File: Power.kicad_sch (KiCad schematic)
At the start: 48 parts, among them SW901 DP3T, U901 BQ24075, U902 TPS7A0533PDBV, U903 LP5907MFX-3.3

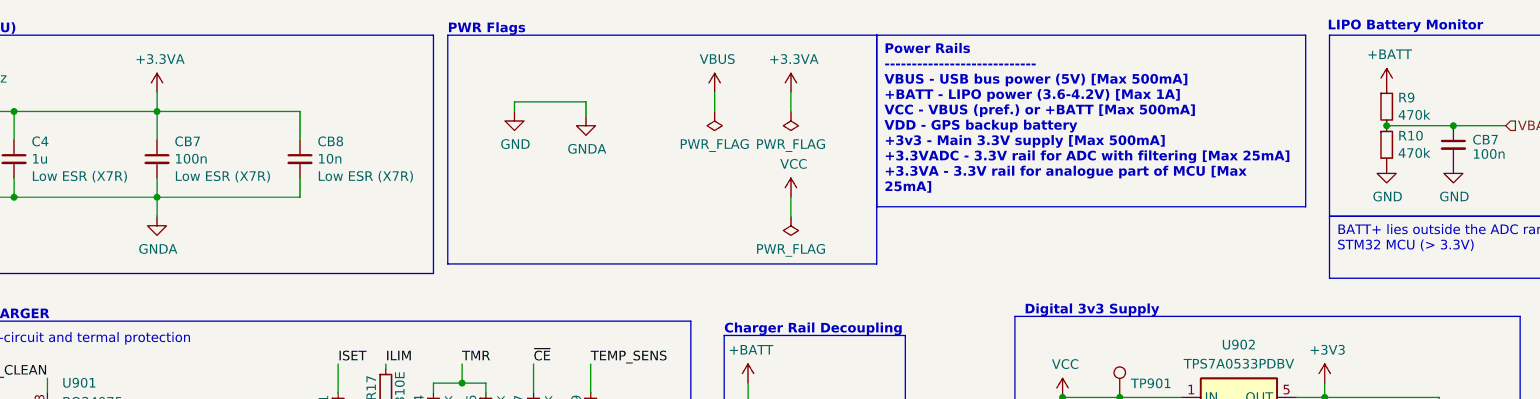
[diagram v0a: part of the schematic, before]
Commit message: (sch) replace GNDA with GND
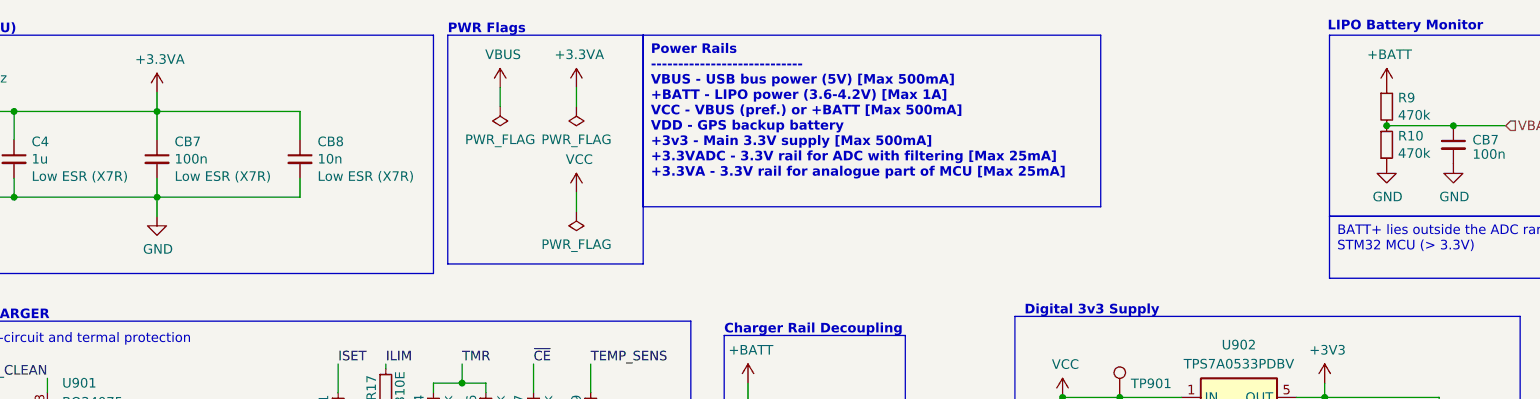
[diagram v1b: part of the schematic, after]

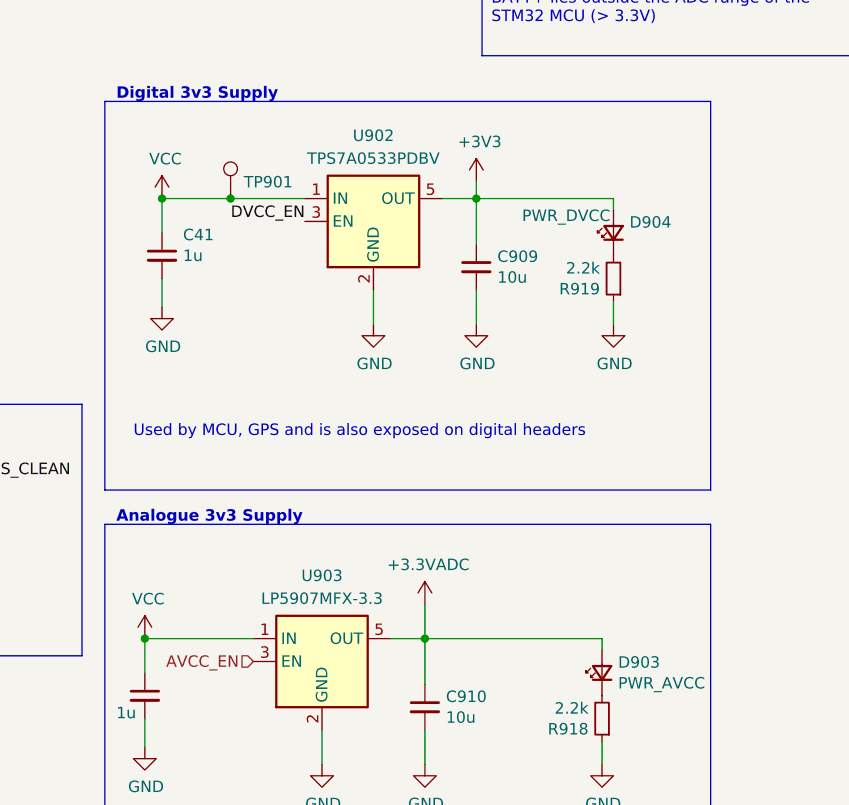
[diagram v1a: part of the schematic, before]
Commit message: (sch) add power test points
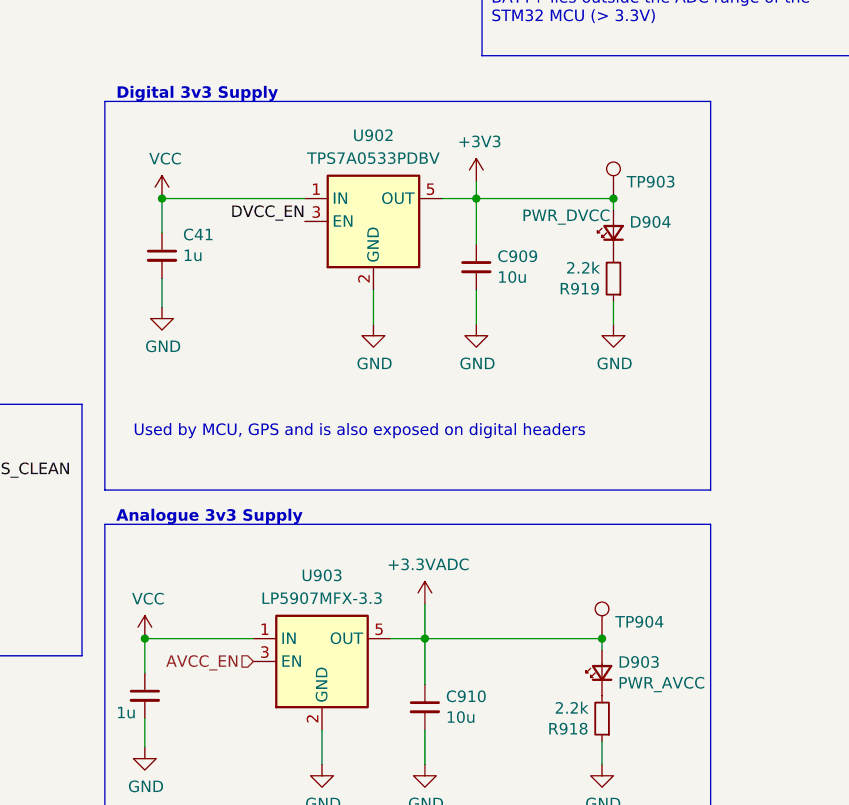
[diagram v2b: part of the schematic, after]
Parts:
- removed TP901: VIN, TestPoint:TestPoint_Pad_D1.0mm, symbol Connector:TestPoint
- added TP903, TP904: VIN, TestPoint:TestPoint_Pad_D1.0mm, symbol Connector:TestPoint
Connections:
- net +3.3VADC: now also TP904.1
- net +3V3: now also TP903.1
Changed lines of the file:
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@@
   (junction (at 57.15 26.67) (diameter 0) (color 0 0 0 0)
   )
+  (junction (at 226.695 113.665) (diameter 0) (color 0 0 0 0)
+  )
   (junction (at 207.01 113.665) (diameter 0) (color 0 0 0 0)
   )
@@
   (junction (at 249.555 28.575) (diameter 0) (color 0 0 0 0)
   )
+  (junction (at 227.965 64.77) (diameter 0) (color 0 0 0 0)
+  )
   (junction (at 212.725 64.77) (diameter 0) (color 0 0 0 0)
   )
@@
   (junction (at 38.1 38.1) (diameter 0) (color 0 0 0 0)
   )
-  (junction (at 185.42 64.77) (diameter 0) (color 0 0 0 0)
-  )
   (junction (at 258.445 28.575) (diameter 0) (color 0 0 0 0)
   )
@@
     (stroke (width 0) (type default))
   )
-  (wire (pts (xy 185.42 64.77) (xy 193.675 64.77))
+  (wire (pts (xy 177.8 64.77) (xy 193.675 64.77))
     (stroke (width 0) (type default))
   )
@@
     (stroke (width 0) (type default))
   )
-  (wire (pts (xy 177.8 64.77) (xy 185.42 64.77))
-    (stroke (width 0) (type default))
-  )
   (wire (pts (xy 107.315 60.325) (xy 107.315 64.135))
     (stroke (width 0) (type default))
@@
     )
   )
+  (symbol (lib_id "Connector:TestPoint") (at 226.695 113.665 0) (unit 1)
+    (in_bom yes) (on_board yes) (dnp no)
+    (property "Reference" "TP904" (at 228.1682 111.8362 0)
+      (effects (font (size 1.27 1.27)) (justify left))
+    )
+    (property "Value" "VIN" (at 228.1682 112.9792 0)
+      (effects (font (size 1.27 1.27)) (justify left) hide)
+    )
+    (property "Footprint" "TestPoint:TestPoint_Pad_D1.0mm" (at 231.775 113.665 0)
+      (effects (font (size 1.27 1.27)) hide)
+    )
+    (property "Datasheet" "~" (at 231.775 113.665 0)
+      (effects (font (size 1.27 1.27)) hide)
+    )
+    (pin "1")
+    (instances
+      (project "kleinvoet"
+        (path "/4185c36c-c66e-4dbd-be5d-841e551f4885/00000000-0000-0000-0000-00005eede770"
+          (reference "TP904") (unit 1)
+        )
+      )
+    )
+  )
   (symbol (lib_id "Device:C_Small") (at 212.725 72.39 0) (unit 1)
     (in_bom yes) (on_board yes) (dnp no)
@@
     )
   )
-  (symbol (lib_id "Connector:TestPoint") (at 185.42 64.77 0) (unit 1)
-    (in_bom yes) (on_board yes) (dnp no)
-    (property "Reference" "TP901" (at 186.8932 62.9412 0)
-      (effects (font (size 1.27 1.27)) (justify left))
-    )
-    (property "Value" "VIN" (at 186.8932 64.0842 0)
-      (effects (font (size 1.27 1.27)) (justify left) hide)
-    )
-    (property "Footprint" "TestPoint:TestPoint_Pad_D1.0mm" (at 190.5 64.77 0)
-      (effects (font (size 1.27 1.27)) hide)
-    )
-    (property "Datasheet" "~" (at 190.5 64.77 0)
-      (effects (font (size 1.27 1.27)) hide)
-    )
-    (pin "1")
-    (instances
-      (project "kleinvoet"
-        (path "/4185c36c-c66e-4dbd-be5d-841e551f4885/00000000-0000-0000-0000-00005eede770"
-          (reference "TP901") (unit 1)
-        )
-      )
-    )
-  )
   (symbol (lib_id "Device:R_Small") (at 78.105 165.1 90) (unit 1)
     (in_bom yes) (on_board yes) (dnp no)
@@
         )
       )
+    )
+  )
+  (symbol (lib_id "Connector:TestPoint") (at 227.965 64.77 0) (unit 1)
+    (in_bom yes) (on_board yes) (dnp no)
+    (property "Reference" "TP903" (at 229.4382 62.9412 0)
+      (effects (font (size 1.27 1.27)) (justify left))
+    )
+    (property "Value" "VIN" (at 229.4382 64.0842 0)
+      (effects (font (size 1.27 1.27)) (justify left) hide)
+    )
+    (property "Footprint" "TestPoint:TestPoint_Pad_D1.0mm" (at 233.045 64.77 0)
+      (effects (font (size 1.27 1.27)) hide)
+    )
+    (property "Datasheet" "~" (at 233.045 64.77 0)
+      (effects (font (size 1.27 1.27)) hide)
+    )
+    (pin "1")
+    (instances
+      (project "kleinvoet"
+        (path "/4185c36c-c66e-4dbd-be5d-841e551f4885/00000000-0000-0000-0000-00005eede770"
+          (reference "TP903") (unit 1)
+        )
+      )

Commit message: change 10u cap from 0805 to 0402
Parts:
- C903, C904, C908, C909, C910: footprint Capacitor_SMD:C_0805_2012Metric_Pad1.18x1.45mm_HandSolder -> Capacitor_SMD:C_0402_1005Metric; MPN C0805C106K9PACTU -> GRM155R60J106ME05D; Mfr. KEMET -> Murata
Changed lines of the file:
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@@
       (effects (font (size 1.27 1.27)) (justify left))
     )
-    (property "Footprint" "Capacitor_SMD:C_0805_2012Metric_Pad1.18x1.45mm_HandSolder" (at 207.01 121.285 0)
+    (property "Footprint" "Capacitor_SMD:C_0402_1005Metric" (at 207.01 121.285 0)
       (effects (font (size 1.27 1.27)) hide)
     )
@@
       (effects (font (size 1.27 1.27)) hide)
     )
-    (property "MPN" "C0805C106K9PACTU" (at 207.01 121.285 0)
-      (effects (font (size 1.27 1.27)) hide)
-    )
-    (property "Mfr." "KEMET" (at 207.01 121.285 0)
+    (property "MPN" "GRM155R60J106ME05D" (at 207.01 121.285 0)
+      (effects (font (size 1.27 1.27)) hide)
+    )
+    (property "Mfr." "Murata" (at 207.01 121.285 0)
       (effects (font (size 1.27 1.27)) hide)
     )
@@
       (effects (font (size 1.27 1.27)) (justify left))
     )
-    (property "Footprint" "Capacitor_SMD:C_0805_2012Metric_Pad1.18x1.45mm_HandSolder" (at 137.16 102.235 0)
+    (property "Footprint" "Capacitor_SMD:C_0402_1005Metric" (at 137.16 102.235 0)
       (effects (font (size 1.27 1.27)) hide)
     )
@@
       (effects (font (size 1.27 1.27)) hide)
     )
-    (property "MPN" "C0805C106K9PACTU" (at 137.16 102.235 0)
-      (effects (font (size 1.27 1.27)) hide)
-    )
-    (property "Mfr." "KEMET" (at 137.16 102.235 0)
+    (property "MPN" "GRM155R60J106ME05D" (at 137.16 102.235 0)
+      (effects (font (size 1.27 1.27)) hide)
+    )
+    (property "Mfr." "Murata" (at 137.16 102.235 0)
       (effects (font (size 1.27 1.27)) hide)
     )
@@
       (effects (font (size 1.27 1.27)) (justify left))
     )
-    (property "Footprint" "Capacitor_SMD:C_0805_2012Metric_Pad1.18x1.45mm_HandSolder" (at 135.89 69.215 0)
+    (property "Footprint" "Capacitor_SMD:C_0402_1005Metric" (at 135.89 69.215 0)
       (effects (font (size 1.27 1.27)) hide)
     )
@@
       (effects (font (size 1.27 1.27)) hide)
     )
-    (property "MPN" "C0805C106K9PACTU" (at 135.89 69.215 0)
-      (effects (font (size 1.27 1.27)) hide)
-    )
-    (property "Mfr." "KEMET" (at 135.89 69.215 0)
+    (property "MPN" "GRM155R60J106ME05D" (at 135.89 69.215 0)
+      (effects (font (size 1.27 1.27)) hide)
+    )
+    (property "Mfr." "Murata" (at 135.89 69.215 0)
       (effects (font (size 1.27 1.27)) hide)
     )
@@
       (effects (font (size 1.27 1.27)) (justify left))
     )
-    (property "Footprint" "Capacitor_SMD:C_0805_2012Metric_Pad1.18x1.45mm_HandSolder" (at 149.86 102.235 0)
+    (property "Footprint" "Capacitor_SMD:C_0402_1005Metric" (at 149.86 102.235 0)
       (effects (font (size 1.27 1.27)) hide)
     )
@@
       (effects (font (size 1.27 1.27)) hide)
     )
-    (property "MPN" "C0805C106K9PACTU" (at 149.86 102.235 0)
-      (effects (font (size 1.27 1.27)) hide)
-    )
-    (property "Mfr." "KEMET" (at 149.86 102.235 0)
+    (property "MPN" "GRM155R60J106ME05D" (at 149.86 102.235 0)
+      (effects (font (size 1.27 1.27)) hide)
+    )
+    (property "Mfr." "Murata" (at 149.86 102.235 0)
       (effects (font (size 1.27 1.27)) hide)
     )
@@
       (effects (font (size 1.27 1.27)) (justify left))
     )
-    (property "Footprint" "Capacitor_SMD:C_0805_2012Metric_Pad1.18x1.45mm_HandSolder" (at 212.725 72.39 0)
+    (property "Footprint" "Capacitor_SMD:C_0402_1005Metric" (at 212.725 72.39 0)
       (effects (font (size 1.27 1.27)) hide)
     )
@@
       (effects (font (size 1.27 1.27)) hide)
     )
-    (property "MPN" "C0805C106K9PACTU" (at 212.725 72.39 0)
-      (effects (font (size 1.27 1.27)) hide)
-    )
-    (property "Mfr." "KEMET" (at 212.725 72.39 0)
-      (effects (font (size 1.27 1.27)) hide)
-    )
+    (property "MPN" "GRM155R60J106ME05D" (at 212.725 72.39 0)
+      (effects (font (size 1.27 1.27)) hide)
+    )
+    (property "Mfr." "Murata" (at 212.725 72.39 0)
+      (effects (font (size 1.27 1.27)) hide)
+    )

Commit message: replace passives with 0402
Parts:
- C4, C41: footprint Capacitor_SMD:C_0603_1608Metric_Pad1.08x0.95mm_HandSolder -> Capacitor_SMD:C_0402_1005Metric; MPN C0603C105K8RACTU -> C0402C105K9PACTU
- FB901, FB903: footprint Inductor_SMD:L_0603_1608Metric_Pad1.05x0.95mm_HandSolder -> Inductor_SMD:L_0402_1005Metric; MPN BLM18KG101TZ1D -> BLM15HD102SN1D
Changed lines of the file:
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@@
       (effects (font (size 1.27 1.27)))
     )
-    (property "Footprint" "Inductor_SMD:L_0603_1608Metric_Pad1.05x0.95mm_HandSolder" (at 30.48 28.448 90)
+    (property "Footprint" "Inductor_SMD:L_0402_1005Metric" (at 30.48 28.448 90)
       (effects (font (size 1.27 1.27)) hide)
     )
@@
       (effects (font (size 1.27 1.27)) hide)
     )
-    (property "MPN" "BLM18KG101TZ1D" (at 30.48 26.67 90)
+    (property "MPN" "BLM15HD102SN1D" (at 30.48 26.67 90)
       (effects (font (size 1.27 1.27)) hide)
     )
@@
       (effects (font (size 1.27 1.27)))
     )
-    (property "Footprint" "Inductor_SMD:L_0603_1608Metric_Pad1.05x0.95mm_HandSolder" (at 144.78 97.663 90)
+    (property "Footprint" "Inductor_SMD:L_0402_1005Metric" (at 144.78 97.663 90)
       (effects (font (size 1.27 1.27)) hide)
     )
@@
       (effects (font (size 1.27 1.27)) hide)
     )
-    (property "MPN" "BLM18KG101TZ1D" (at 144.78 95.885 90)
+    (property "MPN" "BLM15HD102SN1D" (at 144.78 95.885 90)
       (effects (font (size 1.27 1.27)) hide)
     )
@@
       (effects (font (size 1.27 1.27)) (justify left))
     )
-    (property "Footprint" "Capacitor_SMD:C_0603_1608Metric_Pad1.08x0.95mm_HandSolder" (at 38.1 33.02 0)
+    (property "Footprint" "Capacitor_SMD:C_0402_1005Metric" (at 38.1 33.02 0)
       (effects (font (size 1.27 1.27)) hide)
     )
@@
       (effects (font (size 1.27 1.27)) (justify left))
     )
-    (property "MPN" "C0603C105K8RACTU" (at 38.1 33.02 0)
+    (property "MPN" "C0402C105K9PACTU" (at 38.1 33.02 0)
       (effects (font (size 1.27 1.27)) hide)
     )
@@
       (effects (font (size 1.27 1.27)) (justify left))
     )
-    (property "Footprint" "Capacitor_SMD:C_0603_1608Metric_Pad1.08x0.95mm_HandSolder" (at 177.8 71.12 0)
+    (property "Footprint" "Capacitor_SMD:C_0402_1005Metric" (at 177.8 71.12 0)
       (effects (font (size 1.27 1.27)) hide)
     )
@@
       (effects (font (size 1.27 1.27)) (justify left) hide)
     )
-    (property "MPN" "C0603C105K8RACTU" (at 177.8 71.12 0)
+    (property "MPN" "C0402C105K9PACTU" (at 177.8 71.12 0)
       (effects (font (size 1.27 1.27)) hide)
     )
@@
       (effects (font (size 1.27 1.27)) (justify left))
     )
-    (property "Footprint" "Capacitor_SMD:C_0603_1608Metric_Pad1.08x0.95mm_HandSolder" (at 175.895 120.015 0)
+    (property "Footprint" "Capacitor_SMD:C_0402_1005Metric" (at 175.895 120.015 0)
       (effects (font (size 1.27 1.27)) hide)
     )
@@
       (effects (font (size 1.27 1.27)) (justify left) hide)
     )
-    (property "MPN" "C0603C105K8RACTU" (at 175.895 120.015 0)
+    (property "MPN" "C0402C105K9PACTU" (at 175.895 120.015 0)
       (effects (font (size 1.27 1.27)) hide)
     )
@@
       (effects (font (size 1.27 1.27)) (justify left))
     )
-    (property "Footprint" "Capacitor_SMD:C_0603_1608Metric_Pad1.08x0.95mm_HandSolder" (at 20.32 31.75 0)
+    (property "Footprint" "Capacitor_SMD:C_0402_1005Metric" (at 20.32 31.75 0)
       (effects (font (size 1.27 1.27)) hide)
     )
@@
       (effects (font (size 1.27 1.27)) (justify left) hide)
     )
-    (property "MPN" "C0603C105K8RACTU" (at 20.32 31.75 0)
-      (effects (font (size 1.27 1.27)) hide)
-    )
+    (property "MPN" "C0402C105K9PACTU" (at 20.32 31.75 0)
+      (effects (font (size 1.27 1.27)) hide)
+    )

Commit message: (sch) fix BQ25125 3D model
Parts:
- U901: footprint Package_DFN_QFN:VQFN-16-1EP_3x3mm_P0.5mm_EP1.6x1.6mm -> grootvoet:VQFN-16-1EP_3x3mm_P0.5mm_EP1.68x1.68mm_ThermalVias
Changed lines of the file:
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@@
       (effects (font (size 1.27 1.27)) (justify left))
     )
-    (property "Footprint" "Package_DFN_QFN:VQFN-16-1EP_3x3mm_P0.5mm_EP1.6x1.6mm" (at 50.165 93.345 0)
+    (property "Footprint" "grootvoet:VQFN-16-1EP_3x3mm_P0.5mm_EP1.68x1.68mm_ThermalVias" (at 50.165 93.345 0)
       (effects (font (size 1.27 1.27)) (justify left) hide)
     )

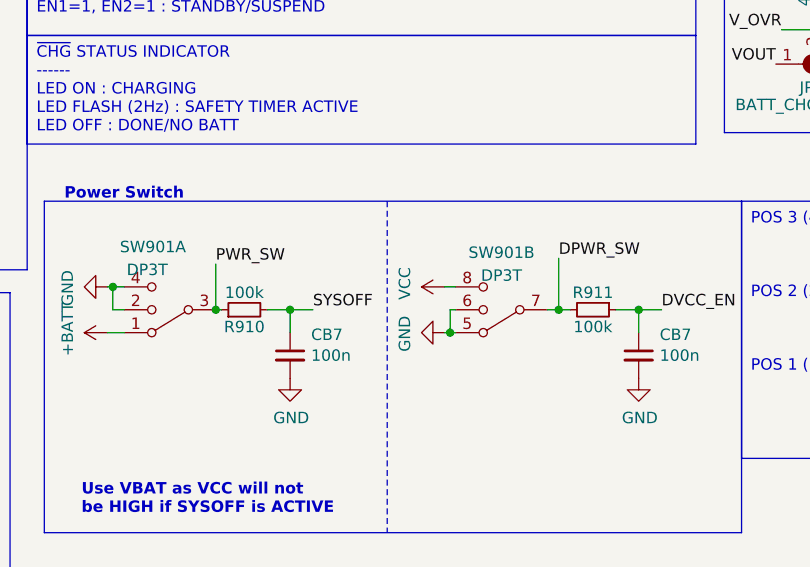
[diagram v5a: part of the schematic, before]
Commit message: (pcb) route power
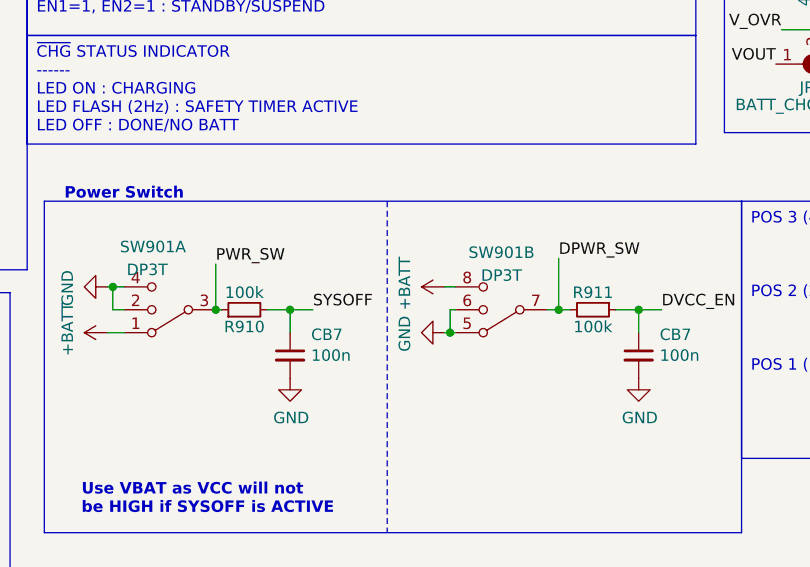
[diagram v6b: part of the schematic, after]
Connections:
- net +BATT: now also SW901.8
- net VCC: no longer SW901.8
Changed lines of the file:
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@@
-    )
-  )
-  (symbol (lib_id "power:VCC") (at 100.33 162.56 90) (unit 1)
-    (in_bom yes) (on_board yes) (dnp no)
-    (property "Reference" "#PWR0938" (at 104.14 162.56 0)
-      (effects (font (size 1.27 1.27)) hide)
-    )
-    (property "Value" "VCC" (at 95.9358 162.179 0)
-      (effects (font (size 1.27 1.27)))
-    )
-    (property "Footprint" "" (at 100.33 162.56 0)
-      (effects (font (size 1.27 1.27)) hide)
-    )
-    (property "Datasheet" "" (at 100.33 162.56 0)
-      (effects (font (size 1.27 1.27)) hide)
-    )
-    (pin "1")
-    (instances
-      (project "kleinvoet"
-        (path "/4185c36c-c66e-4dbd-be5d-841e551f4885/00000000-0000-0000-0000-00005eede770"
-          (reference "#PWR0938") (unit 1)
-        )
-      )
     )
   )
@@
         )
       )
+    )
+  )
+  (symbol (lib_id "power:+BATT") (at 100.33 162.56 90) (unit 1)
+    (in_bom yes) (on_board yes) (dnp no)
+    (property "Reference" "#PWR014" (at 104.14 162.56 0)
+      (effects (font (size 1.27 1.27)) hide)
+    )
+    (property "Value" "+BATT" (at 95.9358 162.179 0)
+      (effects (font (size 1.27 1.27)))
+    )
+    (property "Footprint" "" (at 100.33 162.56 0)
+      (effects (font (size 1.27 1.27)) hide)
+    )
+    (property "Datasheet" "" (at 100.33 162.56 0)
+      (effects (font (size 1.27 1.27)) hide)
+    )
+    (pin "1")
+    (instances
+      (project "kleinvoet"
+        (path "/4185c36c-c66e-4dbd-be5d-841e551f4885/00000000-0000-0000-0000-00005eede770"
+          (reference "#PWR014") (unit 1)
+        )
+      )
